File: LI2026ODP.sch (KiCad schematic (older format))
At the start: 4 parts, among them J1 9-1437539-2, U1 LM2936MPX-3.0_NOPB, U2 STM32G0B1KET6, U3 max6921aui

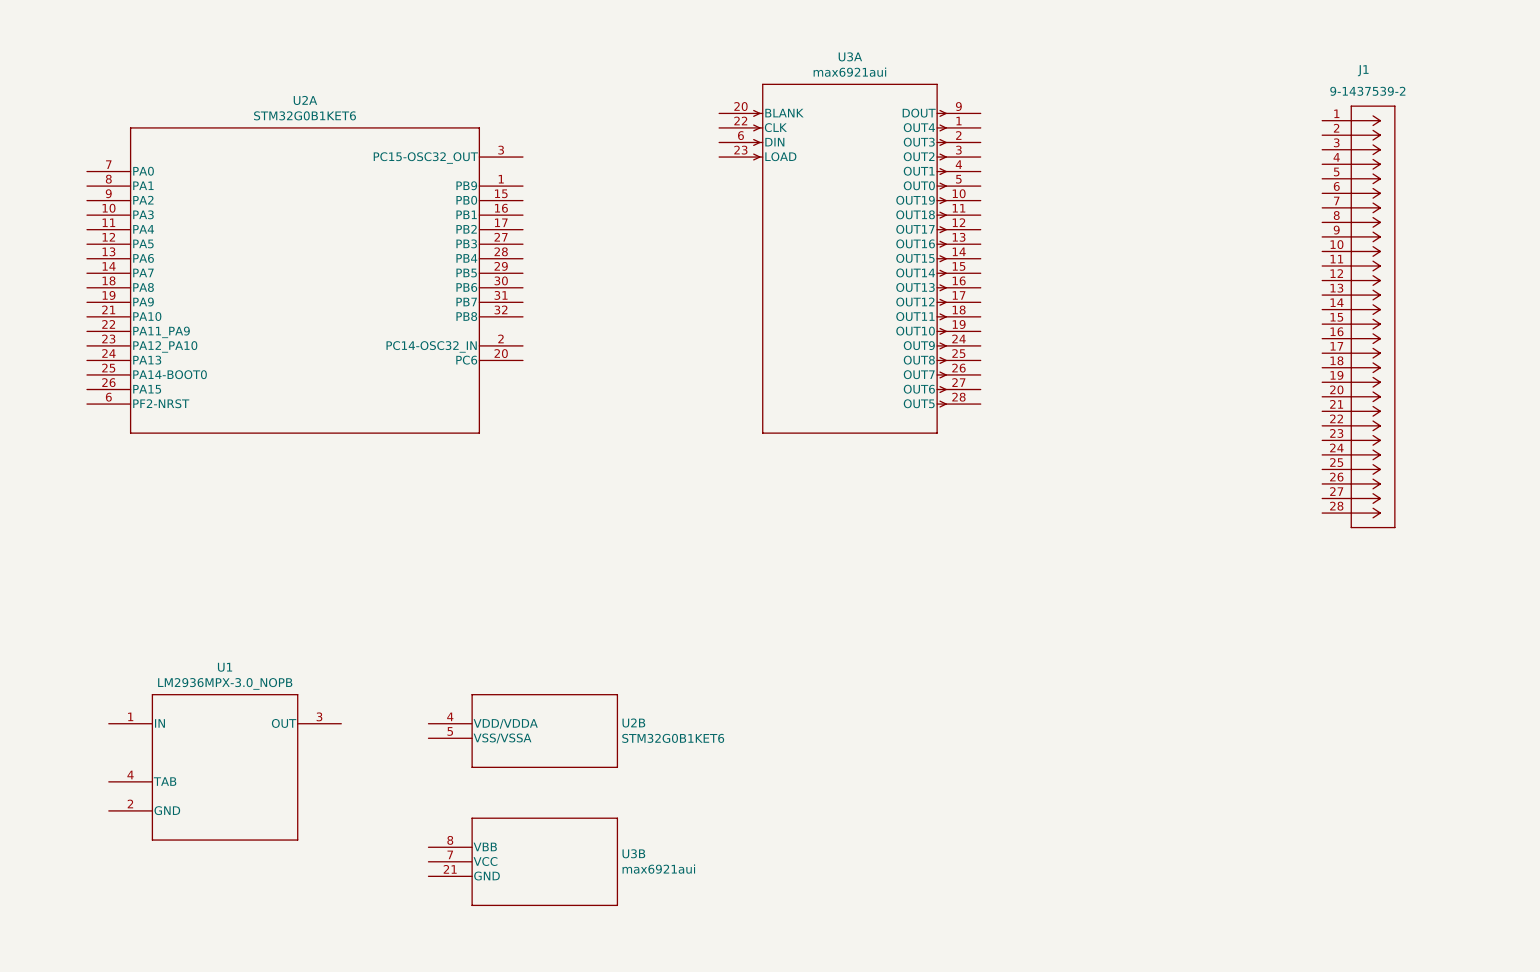
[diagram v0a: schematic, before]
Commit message: All parts connected.
Waiting for the routing.
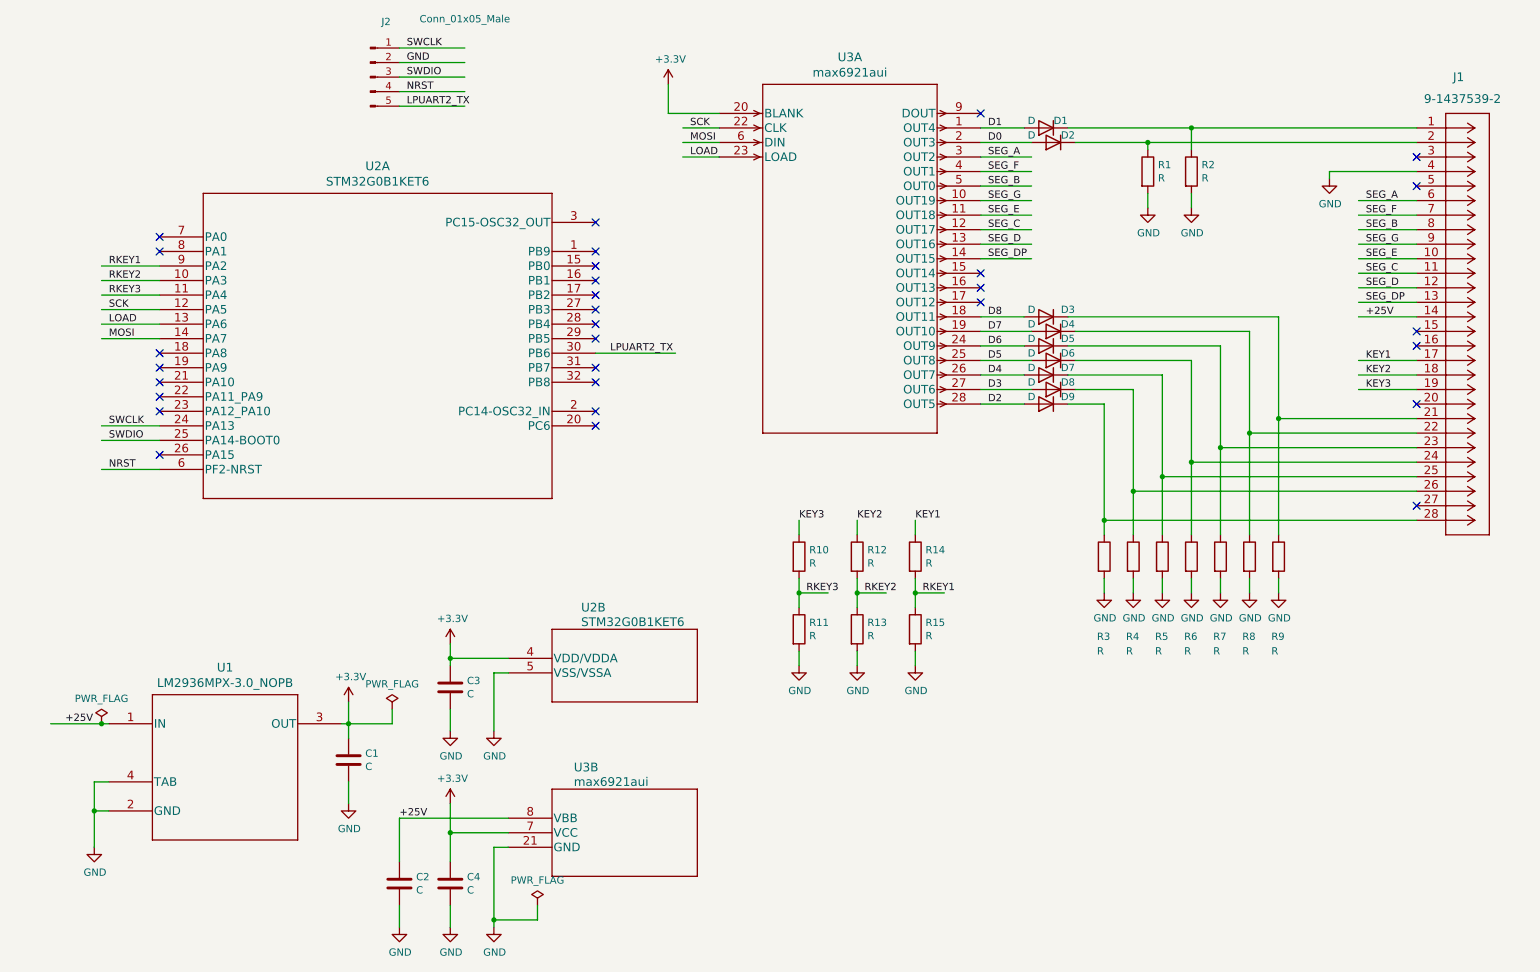
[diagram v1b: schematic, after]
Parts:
- added C1, C2, C3, C4: C, Capacitor_SMD:C_0402_1005Metric, symbol Device:C
- added D1, D2, D3, D4, D5, D6, D7, D8, D9: D, Diode_SMD:D_0402_1005Metric, symbol Device:D
- added J2: Conn_01x05_Male, Connector_PinHeader_2.54mm:PinHeader_1x05_P2.54mm_Vertical, symbol Connector:Conn_01x05_Male
- added R1, R10, R11, R12, R13, R14, R15, R2, R3, R4, R5, R6, R7, R8, R9: R, Resistor_SMD:R_0402_1005Metric, symbol Device:R
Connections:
- net labels added: +25V, +3.3V, D0, D1, D2, D3, D4, D5, D6, D7, D8, GND, KEY1, KEY2, KEY3, LOAD, LPUART2_TX, MOSI, NRST, RKEY1, RKEY2, RKEY3, SCK, SEG_A, SEG_B, SEG_C, SEG_D, SEG_DP, SEG_E, SEG_F, SEG_G, SWCLK, SWDIO
- wire segments 0 -> 139
- no-connect marks 0 -> 30
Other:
- moved on the sheet: J1, U2A, U2B, U3B

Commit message: Change SMD from 1005M to 1608M
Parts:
- C1, C2, C3, C4: footprint Capacitor_SMD:C_0402_1005Metric -> Capacitor_SMD:C_0603_1608Metric_Pad1.08x0.95mm_HandSolder
- D1, D2, D3, D4, D5, D6, D7, D8, D9: footprint Diode_SMD:D_0402_1005Metric -> Diode_SMD:D_0603_1608Metric_Pad1.05x0.95mm_HandSolder
- R1, R10, R11, R12, R13, R14, R15, R2, R3, R4, R5, R6, R7, R8, R9: footprint Resistor_SMD:R_0402_1005Metric -> Resistor_SMD:R_0603_1608Metric_Pad0.98x0.95mm_HandSolder
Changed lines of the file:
@@
 F 0 "D1" H 7650 1800 50  0000 C CNN
 F 1 "D" H 7850 1800 50  0000 C CNN
-F 2 "Diode_SMD:D_0402_1005Metric" H 7750 1850 50  0001 C CNN
+F 2 "Diode_SMD:D_0603_1608Metric_Pad1.05x0.95mm_HandSolder" H 7750 1850 50  0001 C CNN
 F 3 "~" H 7750 1850 50  0001 C CNN
 	1    7750 1850
@@
 F 0 "D2" H 7700 1900 50  0000 C CNN
 F 1 "D" H 7950 1900 50  0000 C CNN
-F 2 "Diode_SMD:D_0402_1005Metric" H 7800 1950 50  0001 C CNN
+F 2 "Diode_SMD:D_0603_1608Metric_Pad1.05x0.95mm_HandSolder" H 7800 1950 50  0001 C CNN
 F 3 "~" H 7800 1950 50  0001 C CNN
 	1    7800 1950
@@
 F 0 "D3" H 7600 3100 50  0000 C CNN
 F 1 "D" H 7850 3100 50  0000 C CNN
-F 2 "Diode_SMD:D_0402_1005Metric" H 7750 3150 50  0001 C CNN
+F 2 "Diode_SMD:D_0603_1608Metric_Pad1.05x0.95mm_HandSolder" H 7750 3150 50  0001 C CNN
 F 3 "~" H 7750 3150 50  0001 C CNN
 	1    7750 3150
@@
 F 0 "D4" H 7700 3200 50  0000 C CNN
 F 1 "D" H 7950 3200 50  0000 C CNN
-F 2 "Diode_SMD:D_0402_1005Metric" H 7800 3250 50  0001 C CNN
+F 2 "Diode_SMD:D_0603_1608Metric_Pad1.05x0.95mm_HandSolder" H 7800 3250 50  0001 C CNN
 F 3 "~" H 7800 3250 50  0001 C CNN
 	1    7800 3250
@@
 F 0 "D5" H 7600 3300 50  0000 C CNN
 F 1 "D" H 7850 3300 50  0000 C CNN
-F 2 "Diode_SMD:D_0402_1005Metric" H 7750 3350 50  0001 C CNN
+F 2 "Diode_SMD:D_0603_1608Metric_Pad1.05x0.95mm_HandSolder" H 7750 3350 50  0001 C CNN
 F 3 "~" H 7750 3350 50  0001 C CNN
 	1    7750 3350
@@
 F 0 "D6" H 7700 3400 50  0000 C CNN
 F 1 "D" H 7950 3400 50  0000 C CNN
-F 2 "Diode_SMD:D_0402_1005Metric" H 7800 3450 50  0001 C CNN
+F 2 "Diode_SMD:D_0603_1608Metric_Pad1.05x0.95mm_HandSolder" H 7800 3450 50  0001 C CNN
 F 3 "~" H 7800 3450 50  0001 C CNN
 	1    7800 3450
@@
 F 0 "D7" H 7600 3500 50  0000 C CNN
 F 1 "D" H 7850 3500 50  0000 C CNN
-F 2 "Diode_SMD:D_0402_1005Metric" H 7750 3550 50  0001 C CNN
+F 2 "Diode_SMD:D_0603_1608Metric_Pad1.05x0.95mm_HandSolder" H 7750 3550 50  0001 C CNN
 F 3 "~" H 7750 3550 50  0001 C CNN
 	1    7750 3550
@@
 F 0 "D8" H 7700 3600 50  0000 C CNN
 F 1 "D" H 7950 3600 50  0000 C CNN
-F 2 "Diode_SMD:D_0402_1005Metric" H 7800 3650 50  0001 C CNN
+F 2 "Diode_SMD:D_0603_1608Metric_Pad1.05x0.95mm_HandSolder" H 7800 3650 50  0001 C CNN
 F 3 "~" H 7800 3650 50  0001 C CNN
 	1    7800 3650
@@
 F 0 "D9" H 7600 3700 50  0000 C CNN
 F 1 "D" H 7850 3700 50  0000 C CNN
-F 2 "Diode_SMD:D_0402_1005Metric" H 7750 3750 50  0001 C CNN
+F 2 "Diode_SMD:D_0603_1608Metric_Pad1.05x0.95mm_HandSolder" H 7750 3750 50  0001 C CNN
 F 3 "~" H 7750 3750 50  0001 C CNN
 	1    7750 3750
@@
 F 0 "R1" H 8520 2196 50  0000 L CNN
 F 1 "R" H 8520 2105 50  0000 L CNN
-F 2 "Resistor_SMD:R_0402_1005Metric" V 8380 2150 50  0001 C CNN
+F 2 "Resistor_SMD:R_0603_1608Metric_Pad0.98x0.95mm_HandSolder" V 8380 2150 50  0001 C CNN
 F 3 "~" H 8450 2150 50  0001 C CNN
 	1    8450 2150
@@
 F 0 "R2" H 8820 2196 50  0000 L CNN
 F 1 "R" H 8820 2105 50  0000 L CNN
-F 2 "Resistor_SMD:R_0402_1005Metric" V 8680 2150 50  0001 C CNN
+F 2 "Resistor_SMD:R_0603_1608Metric_Pad0.98x0.95mm_HandSolder" V 8680 2150 50  0001 C CNN
 F 3 "~" H 8750 2150 50  0001 C CNN
 	1    8750 2150
@@
 F 0 "R3" H 8100 4250 50  0000 L CNN
 F 1 "R" H 8100 4150 50  0000 L CNN
-F 2 "Resistor_SMD:R_0402_1005Metric" V 8080 4800 50  0001 C CNN
+F 2 "Resistor_SMD:R_0603_1608Metric_Pad0.98x0.95mm_HandSolder" V 8080 4800 50  0001 C CNN
 F 3 "~" H 8150 4800 50  0001 C CNN
 	1    8150 4800
@@
 F 0 "R4" H 8300 4250 50  0000 L CNN
 F 1 "R" H 8300 4150 50  0000 L CNN
-F 2 "Resistor_SMD:R_0402_1005Metric" V 8280 4800 50  0001 C CNN
+F 2 "Resistor_SMD:R_0603_1608Metric_Pad0.98x0.95mm_HandSolder" V 8280 4800 50  0001 C CNN
 F 3 "~" H 8350 4800 50  0001 C CNN
 	1    8350 4800
@@
 F 0 "R5" H 8500 4250 50  0000 L CNN
 F 1 "R" H 8500 4150 50  0000 L CNN
-F 2 "Resistor_SMD:R_0402_1005Metric" V 8480 4800 50  0001 C CNN
+F 2 "Resistor_SMD:R_0603_1608Metric_Pad0.98x0.95mm_HandSolder" V 8480 4800 50  0001 C CNN
 F 3 "~" H 8550 4800 50  0001 C CNN
 	1    8550 4800
@@
 F 0 "R6" H 8700 4250 50  0000 L CNN
 F 1 "R" H 8700 4150 50  0000 L CNN
-F 2 "Resistor_SMD:R_0402_1005Metric" V 8680 4800 50  0001 C CNN
+F 2 "Resistor_SMD:R_0603_1608Metric_Pad0.98x0.95mm_HandSolder" V 8680 4800 50  0001 C CNN
 F 3 "~" H 8750 4800 50  0001 C CNN
 	1    8750 4800
@@
 F 0 "R7" H 8900 4250 50  0000 L CNN
 F 1 "R" H 8900 4150 50  0000 L CNN
-F 2 "Resistor_SMD:R_0402_1005Metric" V 8880 4800 50  0001 C CNN
+F 2 "Resistor_SMD:R_0603_1608Metric_Pad0.98x0.95mm_HandSolder" V 8880 4800 50  0001 C CNN
 F 3 "~" H 8950 4800 50  0001 C CNN
 	1    8950 4800
@@
 F 0 "R8" H 9100 4250 50  0000 L CNN
 F 1 "R" H 9100 4150 50  0000 L CNN
-F 2 "Resistor_SMD:R_0402_1005Metric" V 9080 4800 50  0001 C CNN
+F 2 "Resistor_SMD:R_0603_1608Metric_Pad0.98x0.95mm_HandSolder" V 9080 4800 50  0001 C CNN
 F 3 "~" H 9150 4800 50  0001 C CNN
 	1    9150 4800
@@
 F 0 "R9" H 9300 4250 50  0000 L CNN
 F 1 "R" H 9300 4150 50  0000 L CNN
-F 2 "Resistor_SMD:R_0402_1005Metric" V 9280 4800 50  0001 C CNN
+F 2 "Resistor_SMD:R_0603_1608Metric_Pad0.98x0.95mm_HandSolder" V 9280 4800 50  0001 C CNN
 F 3 "~" H 9350 4800 50  0001 C CNN
 	1    9350 4800
@@
 F 0 "R14" H 6920 4846 50  0000 L CNN
 F 1 "R" H 6920 4755 50  0000 L CNN
-F 2 "Resistor_SMD:R_0402_1005Metric" V 6780 4800 50  0001 C CNN
+F 2 "Resistor_SMD:R_0603_1608Metric_Pad0.98x0.95mm_HandSolder" V 6780 4800 50  0001 C CNN
 F 3 "~" H 6850 4800 50  0001 C CNN
 	1    6850 4800
@@
 F 0 "R15" H 6920 5346 50  0000 L CNN
 F 1 "R" H 6920 5255 50  0000 L CNN
-F 2 "Resistor_SMD:R_0402_1005Metric" V 6780 5300 50  0001 C CNN
+F 2 "Resistor_SMD:R_0603_1608Metric_Pad0.98x0.95mm_HandSolder" V 6780 5300 50  0001 C CNN
 F 3 "~" H 6850 5300 50  0001 C CNN
 	1    6850 5300
@@
 F 0 "R12" H 6520 4846 50  0000 L CNN
 F 1 "R" H 6520 4755 50  0000 L CNN
-F 2 "Resistor_SMD:R_0402_1005Metric" V 6380 4800 50  0001 C CNN
+F 2 "Resistor_SMD:R_0603_1608Metric_Pad0.98x0.95mm_HandSolder" V 6380 4800 50  0001 C CNN
 F 3 "~" H 6450 4800 50  0001 C CNN
 	1    6450 4800
@@
 F 0 "R13" H 6520 5346 50  0000 L CNN
 F 1 "R" H 6520 5255 50  0000 L CNN
-F 2 "Resistor_SMD:R_0402_1005Metric" V 6380 5300 50  0001 C CNN
+F 2 "Resistor_SMD:R_0603_1608Metric_Pad0.98x0.95mm_HandSolder" V 6380 5300 50  0001 C CNN
 F 3 "~" H 6450 5300 50  0001 C CNN
 	1    6450 5300
@@
 F 0 "R10" H 6120 4846 50  0000 L CNN
 F 1 "R" H 6120 4755 50  0000 L CNN
-F 2 "Resistor_SMD:R_0402_1005Metric" V 5980 4800 50  0001 C CNN
+F 2 "Resistor_SMD:R_0603_1608Metric_Pad0.98x0.95mm_HandSolder" V 5980 4800 50  0001 C CNN
 F 3 "~" H 6050 4800 50  0001 C CNN
 	1    6050 4800
@@
 F 0 "R11" H 6120 5346 50  0000 L CNN
 F 1 "R" H 6120 5255 50  0000 L CNN
-F 2 "Resistor_SMD:R_0402_1005Metric" V 5980 5300 50  0001 C CNN
+F 2 "Resistor_SMD:R_0603_1608Metric_Pad0.98x0.95mm_HandSolder" V 5980 5300 50  0001 C CNN
 F 3 "~" H 6050 5300 50  0001 C CNN
 	1    6050 5300
@@
 F 0 "C4" H 3765 7096 50  0000 L CNN
 F 1 "C" H 3765 7005 50  0000 L CNN
-F 2 "Capacitor_SMD:C_0402_1005Metric" H 3688 6900 50  0001 C CNN
+F 2 "Capacitor_SMD:C_0603_1608Metric_Pad1.08x0.95mm_HandSolder" H 3688 6900 50  0001 C CNN
 F 3 "~" H 3650 7050 50  0001 C CNN
 	1    3650 7050
@@
 F 0 "C2" H 3415 7096 50  0000 L CNN
 F 1 "C" H 3415 7005 50  0000 L CNN
-F 2 "Capacitor_SMD:C_0402_1005Metric" H 3338 6900 50  0001 C CNN
+F 2 "Capacitor_SMD:C_0603_1608Metric_Pad1.08x0.95mm_HandSolder" H 3338 6900 50  0001 C CNN
 F 3 "~" H 3300 7050 50  0001 C CNN
 	1    3300 7050
@@
 F 0 "C3" H 3765 5746 50  0000 L CNN
 F 1 "C" H 3765 5655 50  0000 L CNN
-F 2 "Capacitor_SMD:C_0402_1005Metric" H 3688 5550 50  0001 C CNN
+F 2 "Capacitor_SMD:C_0603_1608Metric_Pad1.08x0.95mm_HandSolder" H 3688 5550 50  0001 C CNN
 F 3 "~" H 3650 5700 50  0001 C CNN
 	1    3650 5700
@@
 F 0 "C1" H 3065 6246 50  0000 L CNN
 F 1 "C" H 3065 6155 50  0000 L CNN
-F 2 "Capacitor_SMD:C_0402_1005Metric" H 2988 6050 50  0001 C CNN
+F 2 "Capacitor_SMD:C_0603_1608Metric_Pad1.08x0.95mm_HandSolder" H 2988 6050 50  0001 C CNN
 F 3 "~" H 2950 6200 50  0001 C CNN
 	1    2950 6200

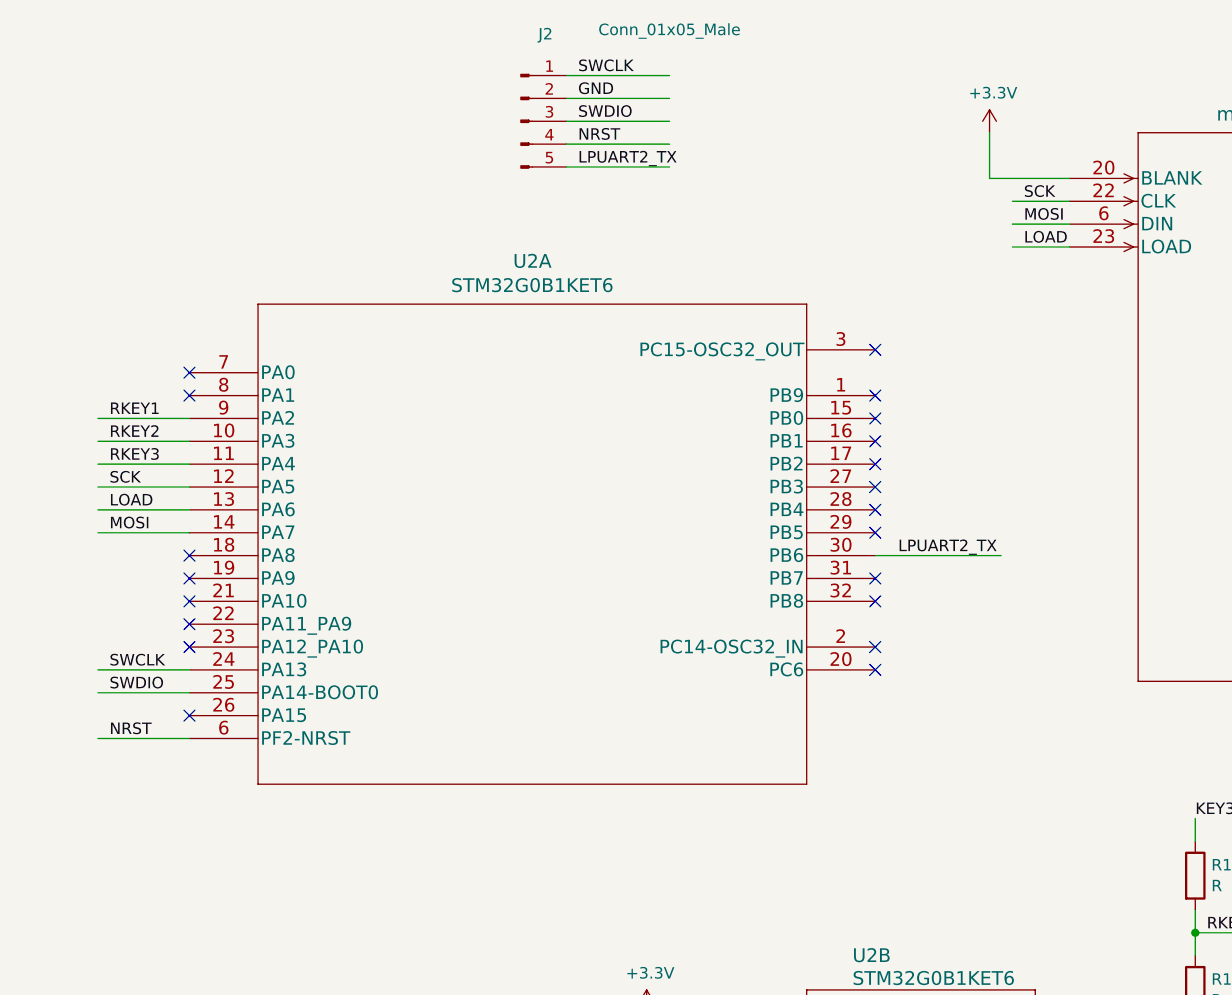
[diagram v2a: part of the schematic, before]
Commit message: Fix the BLANK bug and change layout
- BLANK was incorrectly tied with 3.3v
- Make layer 3 as +3.3v
- Make 25v line as 0.4mm
- Change RKEY1,2,3 pins for the simple layout.
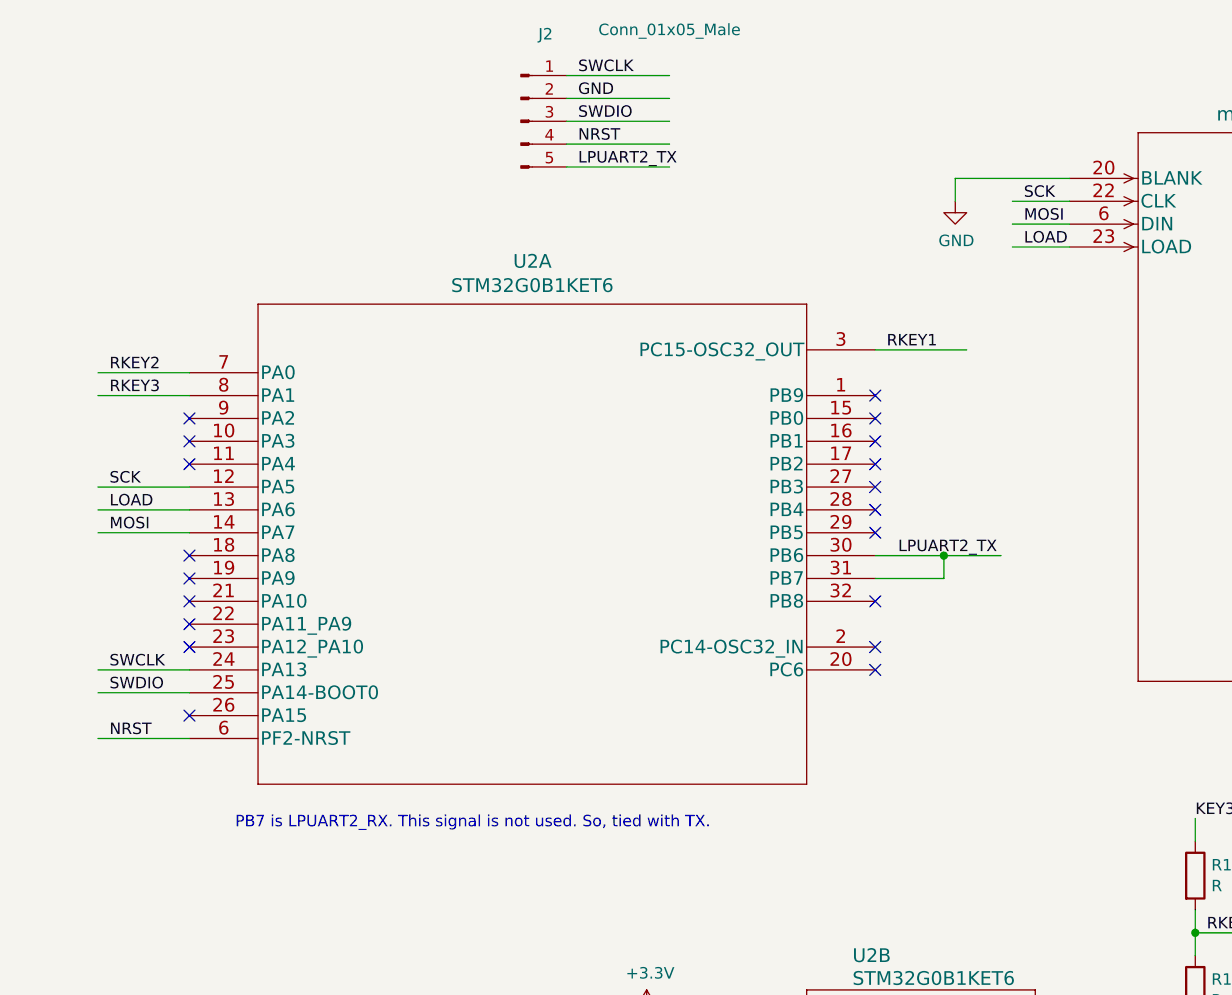
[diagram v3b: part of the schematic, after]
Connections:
- wire segments 139 -> 142
- no-connect marks 30 -> 29
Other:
- note added: "PB7 is LPUART2_RX. This signal is not used. So, tied with TX."
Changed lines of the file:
@@
 	1650 4200 1250 4200
 Wire Wire Line
-	1650 2800 1250 2800
+	5050 2500 4650 2500
 Wire Wire Line
 	1650 3100 1250 3100
 Wire Wire Line
-	1650 3000 1250 3000
+	1650 2700 1250 2700
 Wire Wire Line
 	1650 3200 1250 3200
-Text Label 1300 2800 0    50   ~ 0
-RKEY1
 Text Label 1300 3100 0    50   ~ 0
 SCK
-Text Label 1300 3000 0    50   ~ 0
+Text Label 1300 2700 0    50   ~ 0
 RKEY3
 Text Label 1300 3200 0    50   ~ 0
@@
 Wire Wire Line
 	9700 2150 10300 2150
-$Comp
-L power:+3.3V #PWR03
-U 1 1 61EB0C81
-P 5150 1550
-F 0 "#PWR03" H 5150 1400 50  0001 C CNN
-F 1 "+3.3V" H 5165 1723 50  0000 C CNN
-F 2 "" H 5150 1550 50  0001 C CNN
-F 3 "" H 5150 1550 50  0001 C CNN
-	1    5150 1550
-	1    0    0    -1
-$EndComp
-Wire Wire Line
-	5150 1550 5150 1750
-Wire Wire Line
-	5150 1750 5500 1750
-Wire Wire Line
-	1650 2900 1250 2900
-Text Label 1300 2900 0    50   ~ 0
+Wire Wire Line
+	1650 2600 1250 2600
+Text Label 1300 2600 0    50   ~ 0
 RKEY2
 Wire Wire Line
@@
 NoConn ~ 7300 2950
 NoConn ~ 7300 3050
-NoConn ~ 4650 2500
+NoConn ~ 1650 2800
 NoConn ~ 4650 2700
 NoConn ~ 4650 2800
@@
 NoConn ~ 4650 3200
 NoConn ~ 4650 3300
-NoConn ~ 4650 3500
 NoConn ~ 4650 3600
 NoConn ~ 4650 3800
 NoConn ~ 4650 3900
-NoConn ~ 1650 2600
-NoConn ~ 1650 2700
+NoConn ~ 1650 2900
+NoConn ~ 1650 3000
 NoConn ~ 1650 3400
 NoConn ~ 1650 3500
@@
 $EndComp
 Wire Wire Line
-	4650 3400 5200 3400
+	4650 3400 4950 3400
 Text Label 4750 3400 0    50   ~ 0
 LPUART2_TX
@@
 Text Label 3350 1700 0    50   ~ 0
 LPUART2_TX
+Text Label 4700 2500 0    50   ~ 0
+RKEY1
+Wire Wire Line
+	4650 3500 4950 3500
+Wire Wire Line
+	4950 3500 4950 3400
+Connection ~ 4950 3400
+Wire Wire Line
+	4950 3400 5200 3400
+Text Notes 1850 4600 0    50   ~ 0
+PB7 is LPUART2_RX. This signal is not used. So, tied with TX.
+$Comp
+L power:GND #PWR?
+U 1 1 61E39126
+P 5000 1850
+F 0 "#PWR?" H 5000 1600 50  0001 C CNN
+F 1 "GND" H 5005 1677 50  0000 C CNN
+F 2 "" H 5000 1850 50  0001 C CNN
+F 3 "" H 5000 1850 50  0001 C CNN
+	1    5000 1850
+	1    0    0    -1
+$EndComp
+Wire Wire Line
+	5000 1750 5000 1850
+Wire Wire Line
+	5000 1750 5500 1750
 $EndSCHEMATC
